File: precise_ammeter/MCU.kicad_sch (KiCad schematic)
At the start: 0 parts

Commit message: added mcu part
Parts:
- added C29, C31: 15p, Capacitor_SMD:C_0805_2012Metric, symbol Device:C
- added C30: 4.7u, Capacitor_SMD:C_0805_2012Metric, symbol Device:C
- added C32, C33, C34, C38: 100n, Capacitor_SMD:C_0805_2012Metric, symbol Device:C
- added C35, C37: 1u, Capacitor_SMD:C_0805_2012Metric, symbol Device:C
- added C36: 10n, Capacitor_SMD:C_0805_2012Metric, symbol Device:C
- added D3: LED, LED_SMD:LED_0805_2012Metric, symbol Device:LED
- added D4, D5: ESD, Diode_SMD:D_SOD-923, symbol Diode:ESD9B3.3ST5G
- added J4: Conn_ARM_JTAG_SWD_10, Connector_PinHeader_1.27mm:PinHeader_2x05_P1.27mm_Vertical, symbol Connector:Conn_ARM_JTAG_SWD_10
- added R1: 10k, symbol Device:R
- added R25: 22R, symbol Device:R
- added R5: 1.5k, symbol Device:R
- added U11: STM32G431C6Tx, Package_QFP:LQFP-48_7x7mm_P0.5mm, symbol MCU_ST_STM32G4:STM32G431C6Tx
- added U12: USBLC6-2P6, Package_TO_SOT_SMD:SOT-666, symbol Power_Protection:USBLC6-2P6
- added Y1: 8MHz, symbol Device:Crystal_GND24
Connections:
- new net: C31.1, R25.1, Y1.1
- new net: C29.1, U11.5 (PF0), Y1.3
- new net: D3.2 (A), R5.2
- new net: U11.33 (PA11), U12.1 (I/O1)
- new net: U11.34 (PA12), U12.3 (I/O2)
- new net: D3.1 (K), U11.46 (PB9)
- new net: R25.2, U11.6 (PF1)
- new net +3V3: C30.1, C32.1, C33.1, C34.1, C35.1, C36.1, C37.1, C38.1, J4.1 (VTref), R5.1, U11.1 (VBAT), U11.20 (VREF+), U11.21 (VDDA), U11.24 (VDD), U11.36 (VDD), U11.48 (VDD), U12.5 (VBUS)
- new net Analog_in: D4.2 (A2), U11.9 (PA1)
- new net BOOT0: R1.2, U11.45 (PB8)
- new net GND: C29.2, C30.2, C31.2, C32.2, C33.2, C34.2, C35.2, C36.2, C37.2, C38.2, D4.1 (A1), D5.1 (A1), J4.3 (GND), J4.5 (GND), J4.9 (GNDDetect), R1.1, U11.19 (VSSA), U11.23 (VSS), U11.35 (VSS), U11.47 (VSS), U12.2 (GND), Y1.2, Y1.4
- new net NRST: J4.10 (~{RESET}), U11.7 (PG10)
- new net SWCLK: J4.4 (SWCLK/TCK), U11.38 (PA14)
- new net SWDIO: J4.2 (SWDIO/TMS), U11.37 (PA13)
- new net Stage_1_in: D5.2 (A2), U11.8 (PA0)
- new net USB_D_N: U12.6 (I/O1)
- new net USB_D_P: U12.4 (I/O2)
- no-connect marks 0 -> 2

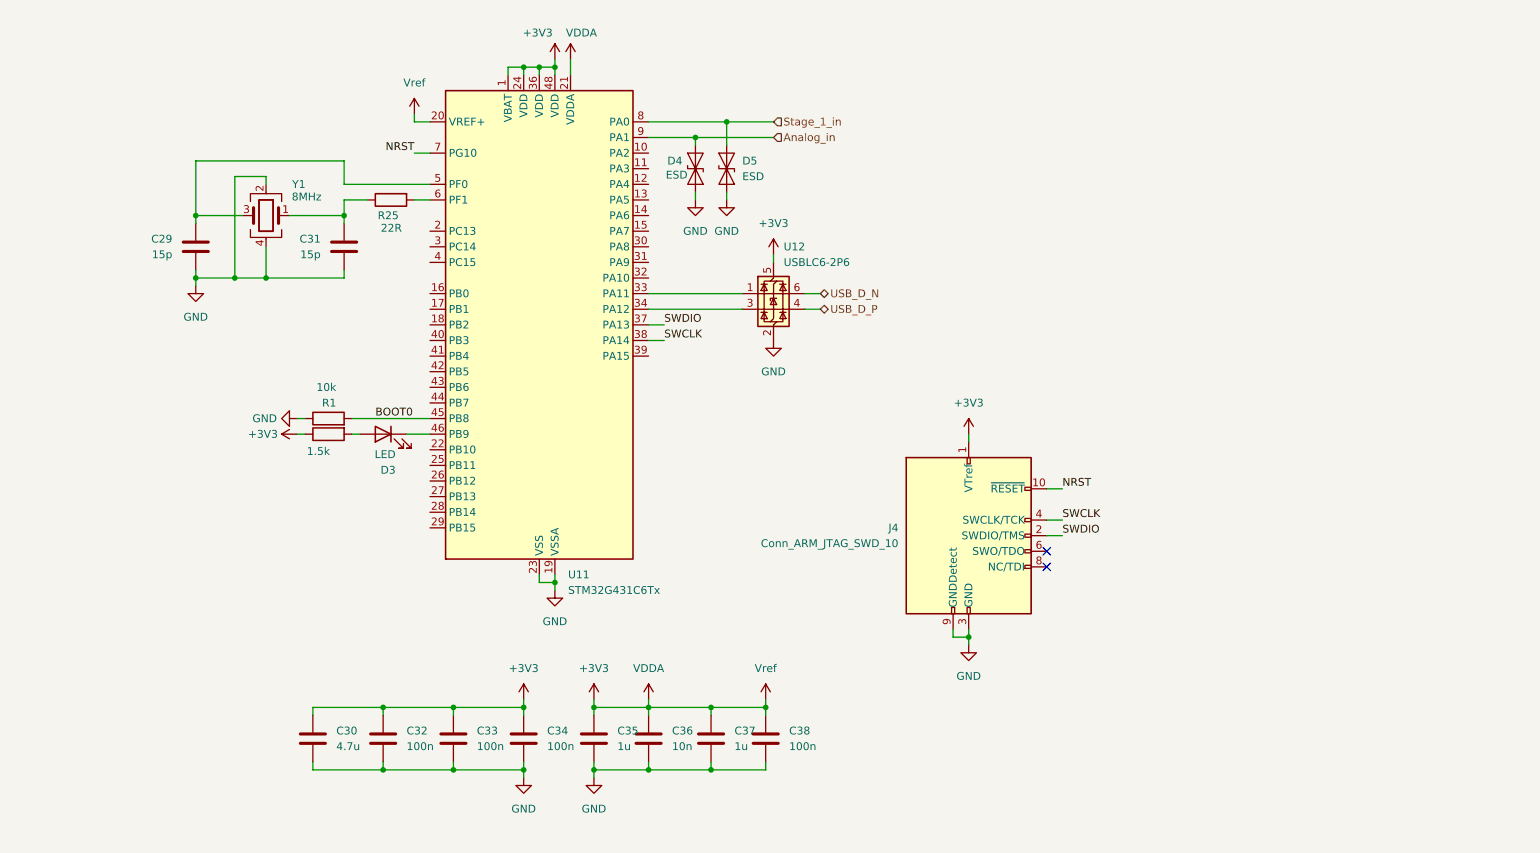
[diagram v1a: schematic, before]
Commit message: fixed mcu schematic
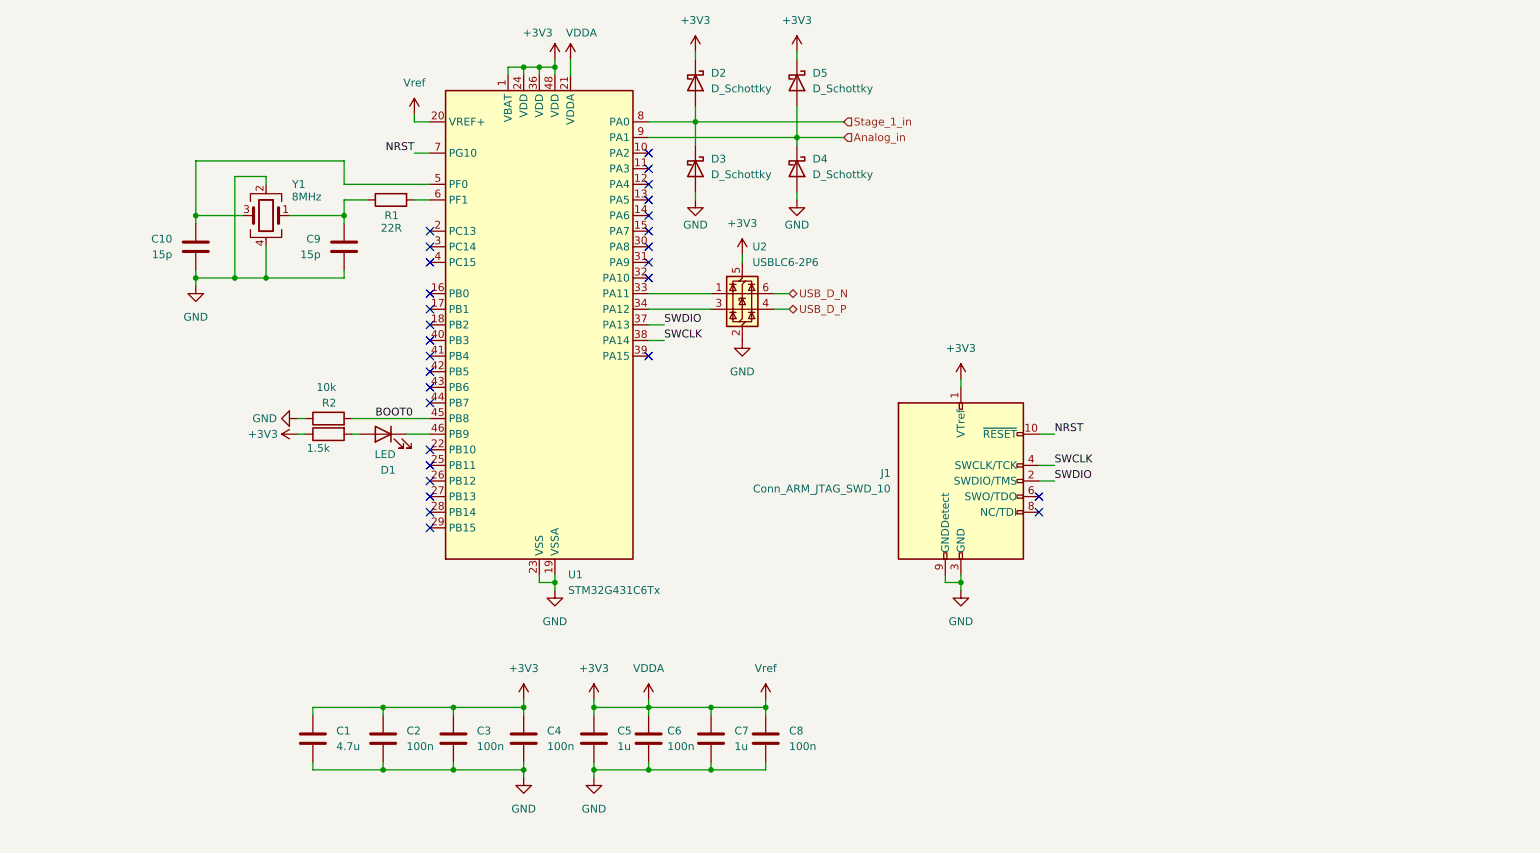
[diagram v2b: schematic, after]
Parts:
- removed D4, D5: ESD, Diode_SMD:D_SOD-923, symbol Diode:ESD9B3.3ST5G
- added D2, D3, D4, D5: D_Schottky, Diode_SMD:D_SOD-123F, symbol Device:D_Schottky
- C6: renamed from C36; value 10n -> 100n
- renumbered C30 to C1, C29 to C10, C32 to C2, C33 to C3, C34 to C4, C35 to C5, C37 to C7, C38 to C8, C31 to C9, D3 to D1, J4 to J1, R5 to R, R25 to R1, R1 to R2, U11 to U1, U12 to U2
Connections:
- net +3V3: now also D2.1 (K), D5.1 (K)
- net Analog_in: now also D4.1 (K), D5.2 (A)
- net GND: now also D3.2 (A), D4.2 (A)
- net Stage_1_in: now also D2.2 (A), D3.1 (K)
- no-connect marks 2 -> 29
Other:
- moved on the sheet: J1, U2

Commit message: Dodano konektor XT30 dla baterii i zrobiono adnotacj diod Schotkiego na schemacie MCU
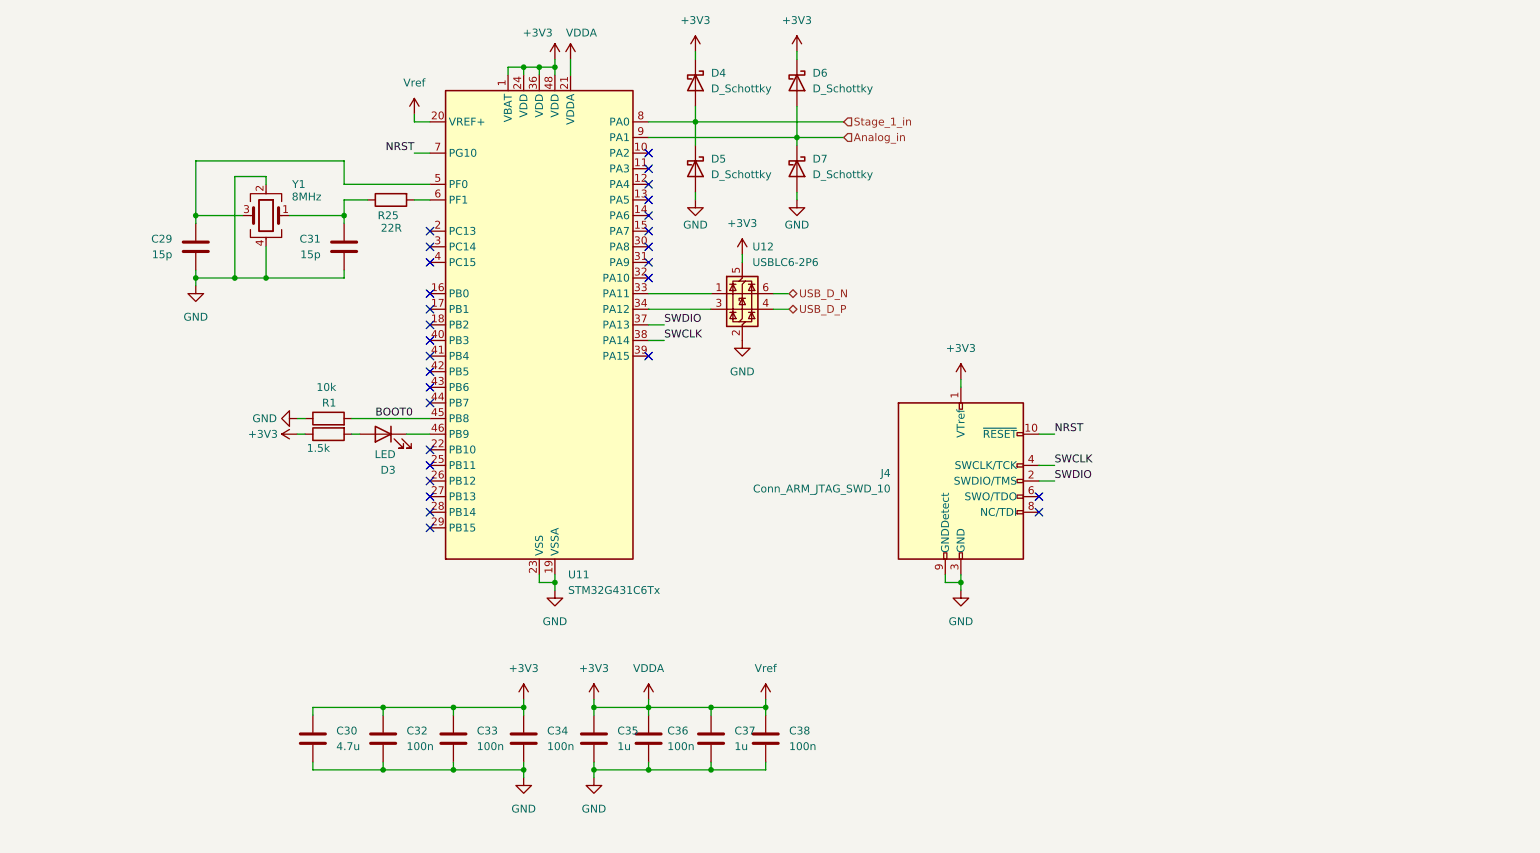
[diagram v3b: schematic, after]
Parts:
- renumbered C10 to C29, C1 to C30, C9 to C31, C2 to C32, C3 to C33, C4 to C34, C5 to C35, C6 to C36, C7 to C37, C8 to C38, D1 to D3, D2 to D4, D3 to D5, D5 to D6, D4 to D7, J1 to J4, R2 to R1, R1 to R25, R to R5, U1 to U11, U2 to U12
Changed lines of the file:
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@@
 		(dnp no)
 		(fields_autoplaced yes)
-		(property "Reference" "#PWR015"
+		(property "Reference" "#PWR067"
 			(at 93.98 45.72 0)
 			(effects
@@
 		(on_board yes)
 		(dnp no)
-		(property "Reference" "#PWR011"
+		(property "Reference" "#PWR066"
 			(at 78.74 93.98 0)
 			(effects
@@
 		(on_board yes)
 		(dnp no)
-		(property "Reference" "#PWR020"
+		(property "Reference" "#PWR0102"
 			(at 139.7 35.56 0)
 			(effects
@@
 				)
 			)
+			(project "precise_ammeter"
+				(path "/7da3b652-85ac-4caa-8d8d-9cad461e9c85/375ae359-eeb3-4ece-be83-a6d2731656da"
+					(reference "#PWR0102")
+					(unit 1)
+				)
+			)
 		)
 	)
@@
 		(dnp no)
 		(fields_autoplaced yes)
-		(property "Reference" "C8"
+		(property "Reference" "C38"
 			(at 154.94 142.2399 0)
 			(effects
@@
 		(dnp no)
 		(fields_autoplaced yes)
-		(property "Reference" "#PWR010"
+		(property "Reference" "#PWR064"
 			(at 58.42 76.2 0)
 			(effects
@@
 		(dnp no)
 		(fields_autoplaced yes)
-		(property "Reference" "#PWR02"
+		(property "Reference" "#PWR074"
 			(at 123.19 156.21 0)
 			(effects
@@
 		(on_board yes)
 		(dnp no)
-		(property "Reference" "R2"
+		(property "Reference" "R1"
 			(at 81.28 88.9001 90)
 			(effects
@@
 		(dnp no)
 		(fields_autoplaced yes)
-		(property "Reference" "C4"
+		(property "Reference" "C34"
 			(at 115.57 142.2399 0)
 			(effects
@@
 		(dnp no)
 		(fields_autoplaced yes)
-		(property "Reference" "#PWR01"
+		(property "Reference" "#PWR069"
 			(at 111.76 156.21 0)
 			(effects
@@
 		(on_board yes)
 		(dnp no)
-		(property "Reference" "R"
+		(property "Reference" "R5"
 			(at 82.042 99.06 90)
 			(effects
@@
 		(dnp no)
 		(fields_autoplaced yes)
-		(property "Reference" "C3"
+		(property "Reference" "C33"
 			(at 104.14 142.2399 0)
 			(effects
@@
 		(dnp no)
 		(fields_autoplaced yes)
-		(property "Reference" "C1"
+		(property "Reference" "C30"
 			(at 81.28 142.2399 0)
 			(effects
@@
 		(dnp no)
 		(fields_autoplaced yes)
-		(property "Reference" "#PWR013"
+		(property "Reference" "#PWR078"
 			(at 151.13 140.97 0)
 			(effects
@@
 		(dnp no)
 		(fields_autoplaced yes)
-		(property "Reference" "#PWR04"
+		(property "Reference" "#PWR081"
 			(at 182.88 88.9 0)
 			(effects
@@
 		(dnp no)
 		(fields_autoplaced yes)
-		(property "Reference" "C7"
+		(property "Reference" "C37"
 			(at 146.05 142.2399 0)
 			(effects
@@
 		(dnp no)
 		(fields_autoplaced yes)
-		(property "Reference" "#PWR05"
+		(property "Reference" "#PWR071"
 			(at 116.84 125.73 0)
 			(effects
@@
 		(on_board yes)
 		(dnp no)
-		(property "Reference" "C10"
+		(property "Reference" "C29"
 			(at 54.61 62.2299 0)
 			(effects
@@
 		(dnp no)
 		(fields_autoplaced yes)
-		(property "Reference" "#PWR09"
+		(property "Reference" "#PWR082"
 			(at 182.88 125.73 0)
 			(effects
@@
 		(dnp no)
 		(fields_autoplaced yes)
-		(property "Reference" "D3"
+		(property "Reference" "D5"
 			(at 142.24 49.2124 90)
 			(effects
@@
 				)
 			)
+			(project "precise_ammeter"
+				(path "/7da3b652-85ac-4caa-8d8d-9cad461e9c85/375ae359-eeb3-4ece-be83-a6d2731656da"
+					(reference "D5")
+					(unit 1)
+				)
+			)
 		)
 	)
@@
 		(dnp no)
 		(fields_autoplaced yes)
-		(property "Reference" "C9"
+		(property "Reference" "C31"
 			(at 78.74 62.2299 0)
 			(effects
@@
 		(on_board yes)
 		(dnp no)
-		(property "Reference" "#PWR014"
+		(property "Reference" "#PWR072"
 			(at 119.38 36.83 0)
 			(effects
@@
 		(on_board yes)
 		(dnp no)
-		(property "Reference" "#PWR021"
+		(property "Reference" "#PWR0101"
 			(at 156.21 35.56 0)
 			(effects
@@
 				)
 			)
+			(project "precise_ammeter"
+				(path "/7da3b652-85ac-4caa-8d8d-9cad461e9c85/375ae359-eeb3-4ece-be83-a6d2731656da"
+					(reference "#PWR0101")
+					(unit 1)
+				)
+			)
 		)
 	)
@@
 		(on_board yes)
 		(dnp no)
-		(property "Reference" "#PWR08"
+		(property "Reference" "#PWR070"
 			(at 116.84 36.83 0)
 			(effects
@@
 		(dnp no)
 		(fields_autoplaced yes)
-		(property "Reference" "J1"
+		(property "Reference" "J4"
 			(at 171.45 100.3299 0)
 			(effects
@@
 		(dnp no)
 		(fields_autoplaced yes)
-		(property "Reference" "#PWR012"
+		(property "Reference" "#PWR075"
 			(at 132.08 140.97 0)
 			(effects
@@
 		(on_board yes)
 		(dnp no)
-		(property "Reference" "C5"
+		(property "Reference" "C35"
 			(at 127 142.2399 0)
 			(effects
@@
 		(on_board yes)
 		(dnp no)
-		(property "Reference" "#PWR07"
+		(property "Reference" "#PWR079"
 			(at 147.32 68.58 0)
 			(effects
@@
 		(dnp no)
 		(fields_autoplaced yes)
-		(property "Reference" "U1"
+		(property "Reference" "U11"
 			(at 118.9833 116.84 0)
 			(effects
@@
 		(dnp no)
 		(fields_autoplaced yes)
-		(property "Reference" "#PWR03"
+		(property "Reference" "#PWR073"
 			(at 123.19 140.97 0)
 			(effects
@@
 		(on_board yes)
 		(dnp no)
-		(property "Reference" "R1"
+		(property "Reference" "R25"
 			(at 91.44 58.4199 90)
 			(effects
@@
 		(on_board yes)
 		(dnp no)
-		(property "Reference" "D1"
+		(property "Reference" "D3"
 			(at 90.932 99.822 0)
 			(effects
@@
 		(dnp no)
 		(fields_autoplaced yes)
-		(property "Reference" "C2"
+		(property "Reference" "C32"
 			(at 92.71 142.2399 0)
 			(effects
@@
 		(on_board yes)
 		(dnp no)
-		(property "Reference" "#PWR019"
+		(property "Reference" "#PWR0103"
 			(at 156.21 62.23 0)
 			(effects
@@
 				)
 			)
+			(project "precise_ammeter"
+				(path "/7da3b652-85ac-4caa-8d8d-9cad461e9c85/375ae359-eeb3-4ece-be83-a6d2731656da"
+					(reference "#PWR0103")
+					(unit 1)
+				)
+			)
 		)
 	)
@@
 		(on_board yes)
 		(dnp no)
-		(property "Reference" "#PWR016"
+		(property "Reference" "#PWR065"
 			(at 68.58 91.44 0)
 			(effects
@@
 		(dnp no)
 		(fields_autoplaced yes)
-		(property "Reference" "#PWR06"
+		(property "Reference" "#PWR080"
 			(at 147.32 85.09 0)
 			(effects
@@
 		(dnp no)
 		(fields_autoplaced yes)
-		(property "Reference" "U2"
+		(property "Reference" "U12"
 			(at 148.9711 63.5 0)
 			(effects
@@
 		(dnp no)
 		(fields_autoplaced yes)
-		(property "Reference" "D4"
+		(property "Reference" "D7"
 			(at 158.75 49.2124 90)
 			(effects
@@
 				)
 			)
+			(project "precise_ammeter"
+				(path "/7da3b652-85ac-4caa-8d8d-9cad461e9c85/375ae359-eeb3-4ece-be83-a6d2731656da"
+					(reference "D7")
+					(unit 1)
+				)
+			)
 		)
 	)
@@
 		(on_board yes)
 		(dnp no)
-		(property "Reference" "#PWR017"
+		(property "Reference" "#PWR0104"
 			(at 139.7 62.23 0)
 			(effects
@@
 				)
 			)
+			(project "precise_ammeter"
+				(path "/7da3b652-85ac-4caa-8d8d-9cad461e9c85/375ae359-eeb3-4ece-be83-a6d2731656da"
+					(reference "#PWR0104")
+					(unit 1)
+				)
+			)
 		)
 	)
@@
 		(on_board yes)
 		(dnp no)
-		(property "Reference" "C6"
+		(property "Reference" "C36"
 			(at 135.128 142.24 0)
 			(effects
@@
 		(dnp no)
 		(fields_autoplaced yes)
-		(property "Reference" "D5"
+		(property "Reference" "D6"
 			(at 158.75 35.2424 90)
 			(effects
@@
 				)
 			)
+			(project "precise_ammeter"
+				(path "/7da3b652-85ac-4caa-8d8d-9cad461e9c85/375ae359-eeb3-4ece-be83-a6d2731656da"
+					(reference "D6")
+					(unit 1)
+				)
+			)
 		)
 	)
@@
 		(dnp no)
 		(fields_autoplaced yes)
-		(property "Reference" "D2"
+		(property "Reference" "D4"
 			(at 142.24 35.2424 90)
 			(effects
@@
 				)
 			)
+			(project "precise_ammeter"
+				(path "/7da3b652-85ac-4caa-8d8d-9cad461e9c85/375ae359-eeb3-4ece-be83-a6d2731656da"
+					(reference "D4")
+					(unit 1)
+				)
+			)
 		)
 	)
@@
 		(dnp no)
 		(fields_autoplaced yes)
-		(property "Reference" "#PWR018"
+		(property "Reference" "#PWR068"
 			(at 111.76 140.97 0)
 			(effects

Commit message: dodano layout
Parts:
- removed Y1: 8MHz, symbol Device:Crystal_GND24
- added Y1: Crystal, Crystal:Crystal_SMD_HC49-SD, symbol Device:Crystal
- C29, C31: footprint Capacitor_SMD:C_0805_2012Metric -> Capacitor_SMD:C_0603_1608Metric_Pad1.08x0.95mm_HandSolder
- C30, C35, C37: footprint Capacitor_SMD:C_0805_2012Metric -> Capacitor_SMD:C_0805_2012Metric_Pad1.18x1.45mm_HandSolder
- C32, C33, C34, C36, C38: value 100n -> 1u; footprint Capacitor_SMD:C_0805_2012Metric -> Capacitor_SMD:C_0805_2012Metric_Pad1.18x1.45mm_HandSolder
- R1, R5: footprint (none) -> Resistor_SMD:R_0805_2012Metric_Pad1.20x1.40mm_HandSolder
- R25: value 22R -> 0; footprint (none) -> Resistor_SMD:R_0805_2012Metric_Pad1.20x1.40mm_HandSolder
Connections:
- net at C31.1, R25.1: now also Y1.2
- net at C29.1, U11.5 (PF0): now also Y1.1

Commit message: dodano skonczone PCB
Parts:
- added C39: 1u, Capacitor_SMD:C_0805_2012Metric_Pad1.18x1.45mm_HandSolder, symbol Device:C
- added R27, R33: 4.7k, Resistor_SMD:R_0805_2012Metric_Pad1.20x1.40mm_HandSolder, symbol Device:R
- added U8: DM-OLED096-636, DM-OLED096-636:MODULE_DM-OLED096-636, symbol DM-OLED096-636:DM-OLED096-636
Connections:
- net +3V3: now also C39.1, R27.2, R33.2, U8.2 (VCC_IN)
- net GND: now also C39.2, U8.1 (GND)
- net SCL: now reaches U11.39 (PA15)
- net SCL: now also R27.1, U8.3 (SCL)
- net SDA: now reaches U11.44 (PB7)
- net SDA: now also R33.1, U8.4 (SDA)
- no-connect marks 29 -> 27
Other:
- moved on the sheet: C29, C30, C31, C32, C33, C34, C35, C36, C37, C38, D3, D4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

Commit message: unknown changes
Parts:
- R1: value 10k -> 1.5k
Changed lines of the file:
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@@
 			)
 		)
-		(property "Value" "10k"
+		(property "Value" "1.5k"
 			(at 59.69 90.1701 90)
 			(effects
